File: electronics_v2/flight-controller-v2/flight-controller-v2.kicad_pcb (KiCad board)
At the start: 2 copper layers, 90 parts, among them J1 Conn_02x05_Odd_Even, J2 USB_B_Micro, J3 Conn_02x03_Odd_Even, J4 Conn_01x05, J5 Conn_01x06, J6 Conn_01x05, SW1 SW_Push, SW2 SW_Push, SW3 SW_Push, SW4 SW_Push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

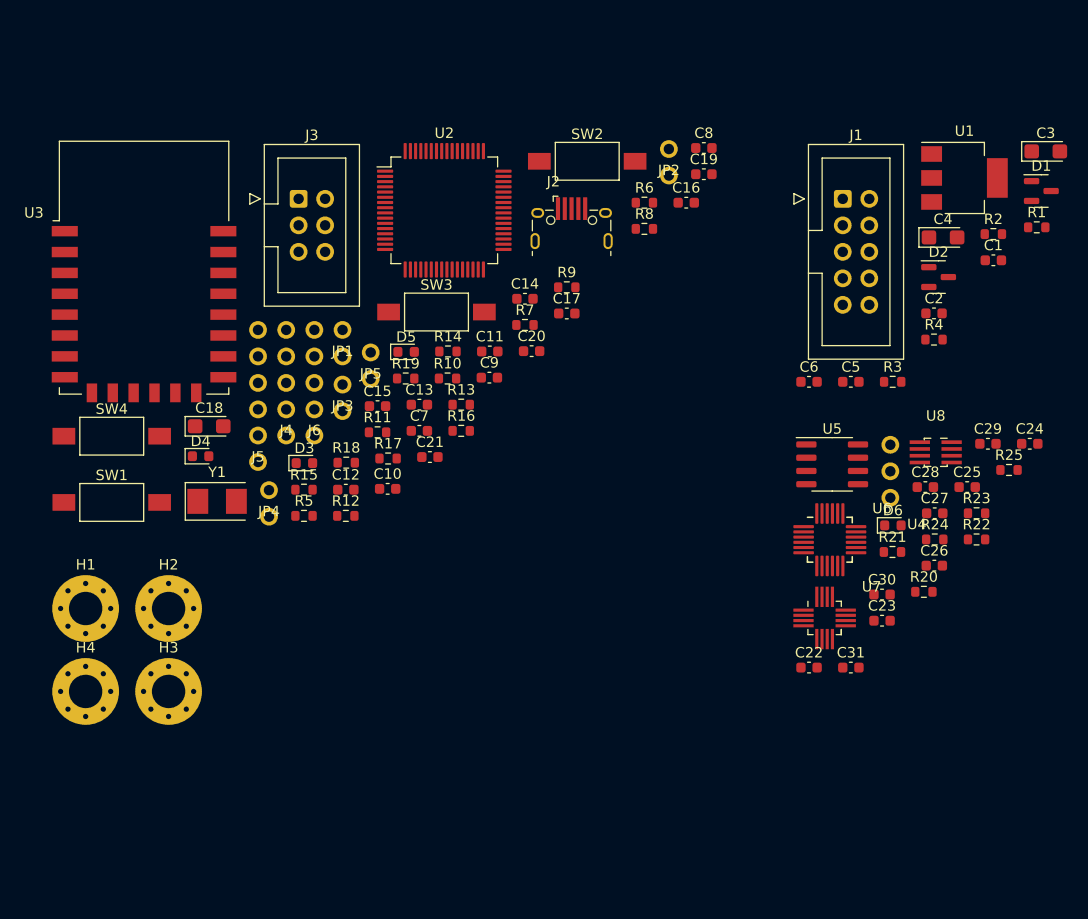
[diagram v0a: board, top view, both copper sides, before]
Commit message: first board cutout and layout
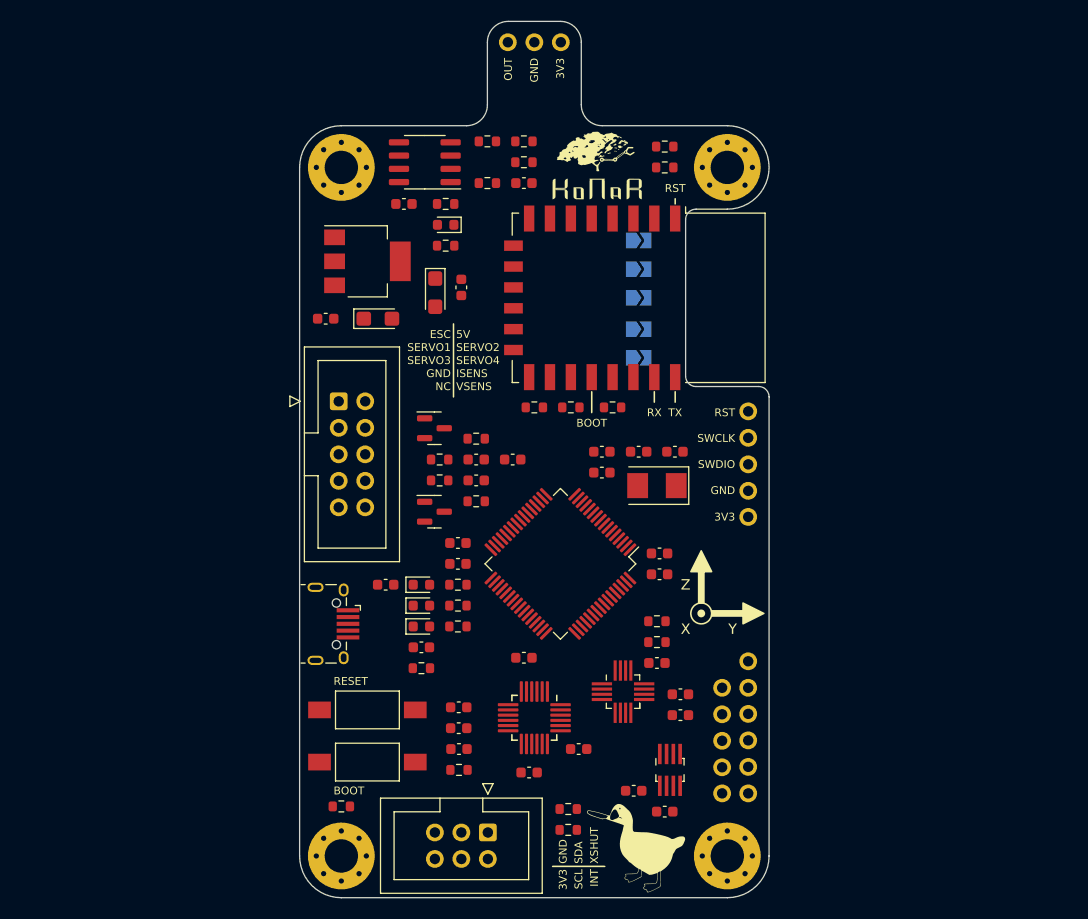
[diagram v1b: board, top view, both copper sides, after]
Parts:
- removed C18: 4u7, Capacitor_Tantalum_SMD:CP_EIA-3216-18_Kemet-A
- removed SW3, SW4: SW_Push, Button_Switch_SMD:SW_SPST_FSMSM
- added G***: LOGO, LOGO, F.Cu at (152.5, 80.5)
- added G***: LOGO, LOGO, F.Cu at (154.6, 145.3)
- added G***: LOGO, LOGO, B.Cu at (146.6, 108.2)
- added G***: LOGO, LOGO, B.Cu at (146.5, 130.0)
- JP1, JP2, JP3, JP4, JP5: footprint goose:tht_pin_01x02 -> Jumper:SolderJumper-2_P1.3mm_Open_TrianglePad1.0x1.5mm; moved to B.Cu
- moved H2 68.2 mm to (165.0, 80.0)
- moved C3 66.0 mm to (131.5, 94.5)
- moved D1 65.8 mm to (136.9, 113.0)
- moved R6 64.8 mm to (128.0, 141.2)
- moved H4 63.5 mm to (165.0, 146.0)
- moved J3 63.4 mm to (142.0, 143.7), turned to -90 degrees
- moved R1 62.2 mm to (137.4, 110.0)
- moved SW2 61.3 mm to (130.5, 137.0)
- moved R20 59.0 mm to (138.0, 83.5)
- moved C22 59.0 mm to (134.0, 83.5), turned to 180 degrees
- moved C2 58.3 mm to (126.5, 94.5), turned to 180 degrees
- moved R22 58.2 mm to (138.0, 87.5), turned to 180 degrees
- moved R8 58.1 mm to (149.8, 143.5), turned to 180 degrees
- moved U1 57.8 mm to (130.5, 89.0)
- moved C24 57.4 mm to (146.0, 138.0)
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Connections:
- net /ucontroller/ESP_GPIO15_CS_TXD2 renamed /ucontroller/ESP_GPIO15
- net Net-(R20-Pad1) renamed /sensors/COMP_P
- U2 pad 24: /power/V_FILTER -> /power/I_FILTER
- U2 pad 25: /power/I_FILTER -> /power/V_FILTER
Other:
- board outline added: 45 x 84 mm
- board text added: "3V3"
- board text added: "5V"
- board text added: "BOOT"
- board text added: "ESC"
- board text added: "GND"
- board text added: "INT"
- board text added: "ISENS"
- board text added: "MRX"
- board text added: "MTX"
- board text added: "NC"
- board text added: "OUT"
- board text added: "RESET"
- board text added: "RST"
- board text added: "RX"
- board text added: "SCL"
- board text added: "SDA"
- board text added: "SERVO1"
- board text added: "SERVO2"
- board text added: "SERVO3"
- board text added: "SERVO4"
- board text added: "SWCLK"
- board text added: "SWDIO"
- board text added: "TX"
- board text added: "UAV TVC Goose Flight Controller V2.0 by Eryk Możdżeń July 2023"
- board text added: "VSENS"
- board text added: "X"
- board text added: "XSHUT"
- board text added: "Y"
- board text added: "Z"
